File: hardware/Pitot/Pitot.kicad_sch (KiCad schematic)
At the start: 28 parts, among them J1 53307-2471, J2 Conn_01x05, J4 Conn_01x08, J5 Conn_01x05, J6 Conn_01x04, J7 Conn_01x04

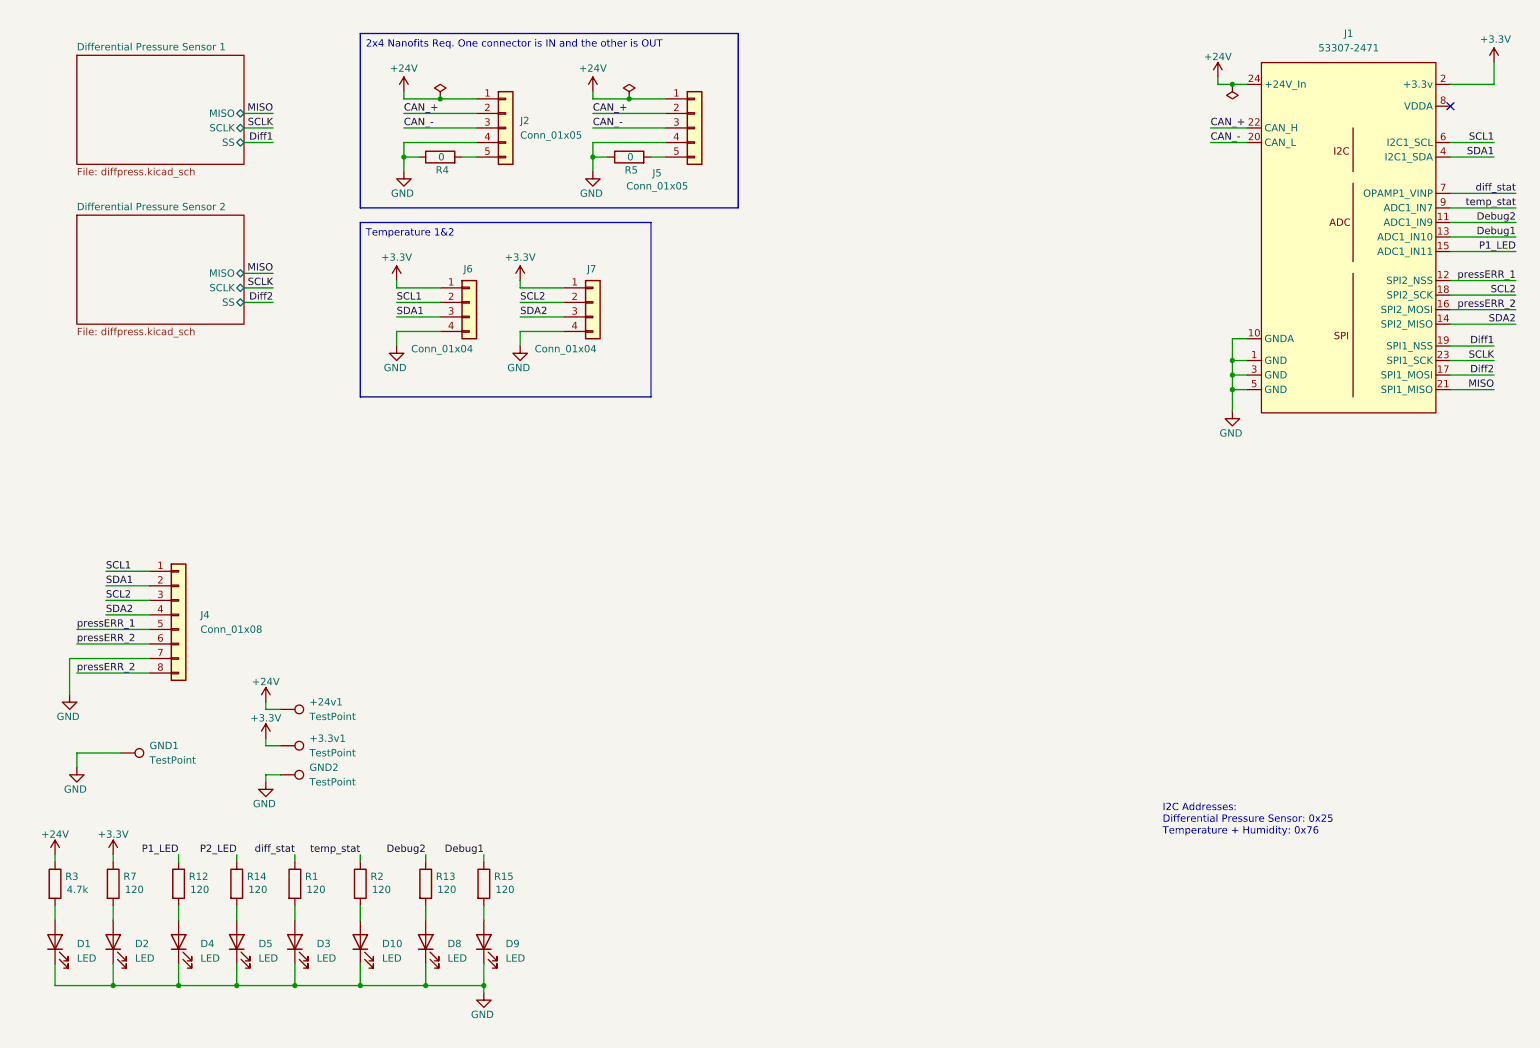
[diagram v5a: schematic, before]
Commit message: Pitot Board Rev B (#3)
* init

* added layout

* ready to review

* finished pitot board

* pitot board ordered, routing+size finished for temperature board so pull??

* finished tempboard silkscreen

* resized temperature board

* poo oo ee

* ughhhhhhhhhhhhhhhhhhghghghhhhhhhhhhhhhhhhhhh

* working i2c on RH board

* cleanup?

* small

* added read me

* fixed mistake

* Fix image filename case in README.md

* Add new line for telemetry components explanation
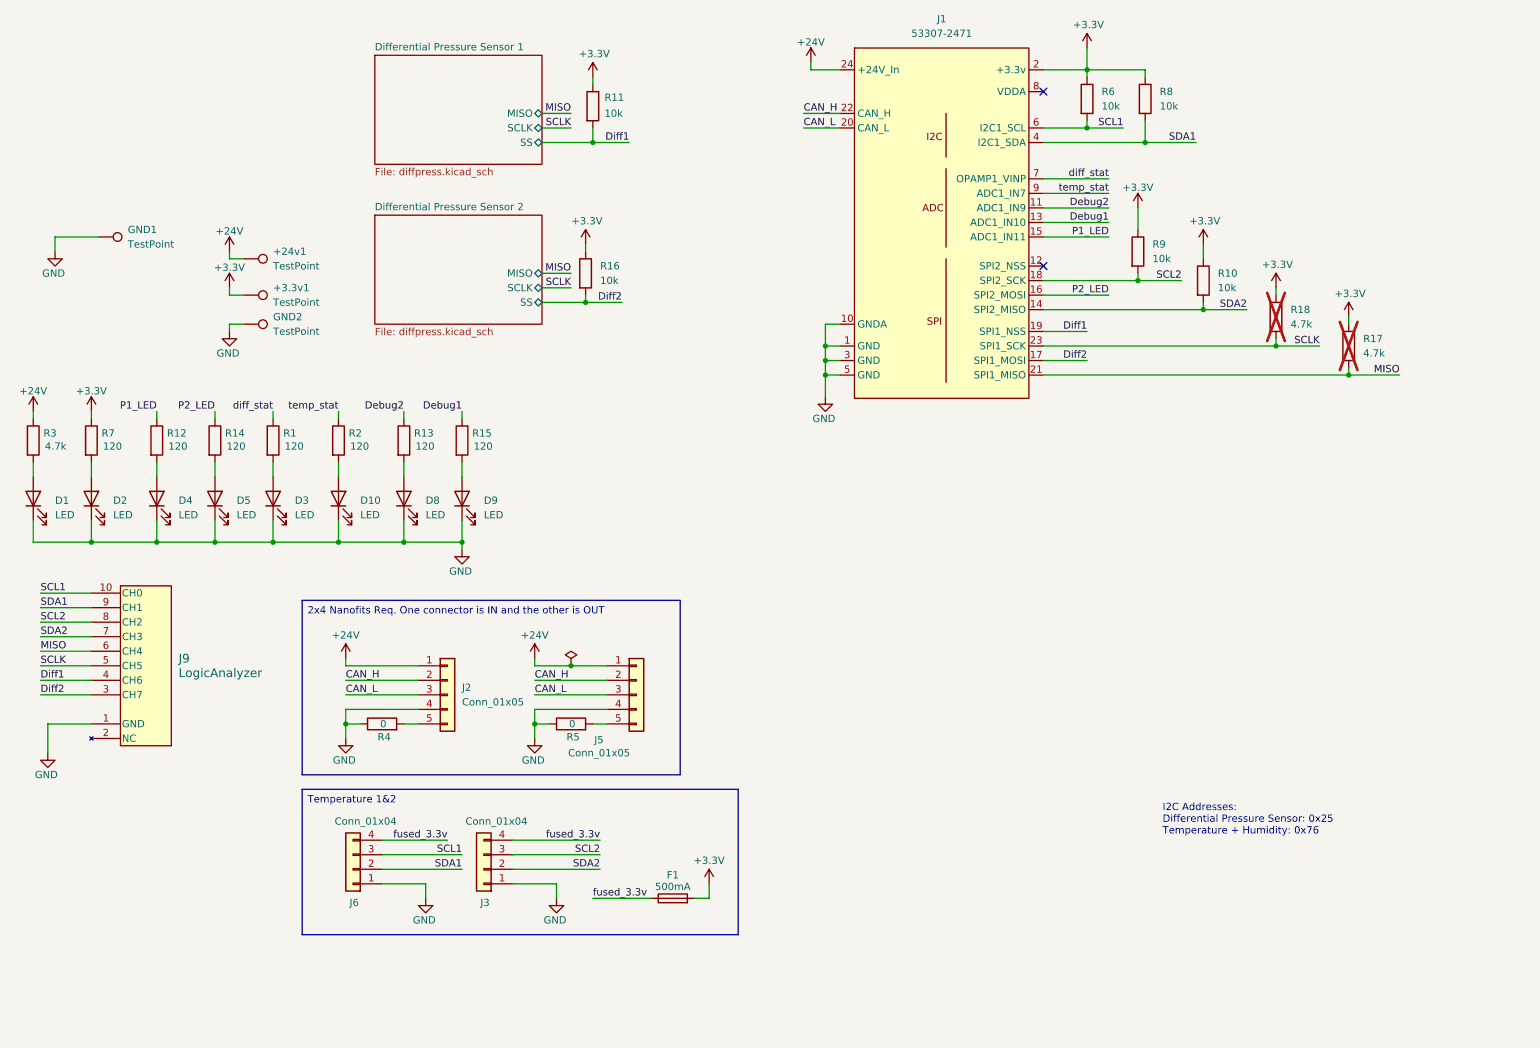
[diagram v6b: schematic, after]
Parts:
- removed J4: Conn_01x08, Connector_PinHeader_2.54mm:PinHeader_2x04_P2.54mm_Vertical, symbol Connector_Generic:Conn_01x08
- removed J7: Conn_01x04, symbol Connector_Generic:Conn_01x04
- added F1: 500mA, Fuse:Fuse_0603_1608Metric_Pad1.05x0.95mm_HandSolder, symbol Device:Fuse
- added J3: Conn_01x04, Connector_Molex:Molex_Nano-Fit_105313-xx04_1x04_P2.50mm_Horizontal, symbol Connector_Generic:Conn_01x04
- added J9: LogicAnalyzer, UTSVT_Connectors:CONN_SFH11-xxxC-D05-ST-XX_SUL, symbol utsvt_connectors:LogicAnalyzer
- added R10, R11, R16, R6, R8, R9: 10k, Resistor_SMD:R_0603_1608Metric_Pad0.98x0.95mm_HandSolder, symbol Device:R
- added R17, R18: 4.7k, Resistor_SMD:R_0603_1608Metric_Pad0.98x0.95mm_HandSolder, symbol Device:R
- +24v1, +3.3v1, GND1, GND2: footprint TestPoint:TestPoint_Pad_1.0x1.0mm -> TestPoint:TestPoint_THTPad_2.0x2.0mm_Drill1.0mm; now left out of the parts list
- J2, J5: footprint (none) -> Connector_Molex:Molex_Nano-Fit_105313-xx05_1x05_P2.50mm_Horizontal; P/N (none) -> 1053131105
- J6: footprint (none) -> Connector_Molex:Molex_Nano-Fit_105313-xx04_1x04_P2.50mm_Horizontal; P/N (none) -> 1053131104
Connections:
- net pressERR_2 is gone; now on net P2_LED: J1.16 (SPI2_MOSI)
- net +3.3V: now also F1.2, R10.1, R11.1, R16.1, R17.1, R18.1, R6.1, R8.1, R9.1; no longer J6.1 (Pin_1)
- net Diff1: now also J9.4 (CH6), R11.2
- net Diff2: now also J9.3 (CH7), R16.2
- net GND: now also J6.1 (Pin_1), J3.1 (Pin_1), J9.1 (GND); no longer J6.4 (Pin_4)
- net MISO: now also J9.6 (CH4), R17.2
- net SCL1: now also J6.3 (Pin_3), J9.10 (CH0), R6.2; no longer J6.2 (Pin_2)
- net SCL2: now also J3.3 (Pin_3), J9.8 (CH2), R9.2
- net SCLK: now also J9.5 (CH5), R18.2
- net SDA1: now also J6.2 (Pin_2), J9.9 (CH1), R8.2; no longer J6.3 (Pin_3)
- net SDA2: now also J3.2 (Pin_2), J9.7 (CH3), R10.2
- net CAN_+ renamed CAN_H
- net CAN_- renamed CAN_L
- net pressERR_1: no longer names the net of J1.12 (SPI2_NSS)
- new net fused_3.3v: F1.1, J3.4 (Pin_4), J6.4 (Pin_4)
- no-connect marks 1 -> 2
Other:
- moved on the sheet: +24v1, +3.3v1, D1, D10, D2, D3, D4, D5, D8, D9, GND1, GND2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
